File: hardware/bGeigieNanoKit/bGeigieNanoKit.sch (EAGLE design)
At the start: 34 parts, among them T1 2SC1815

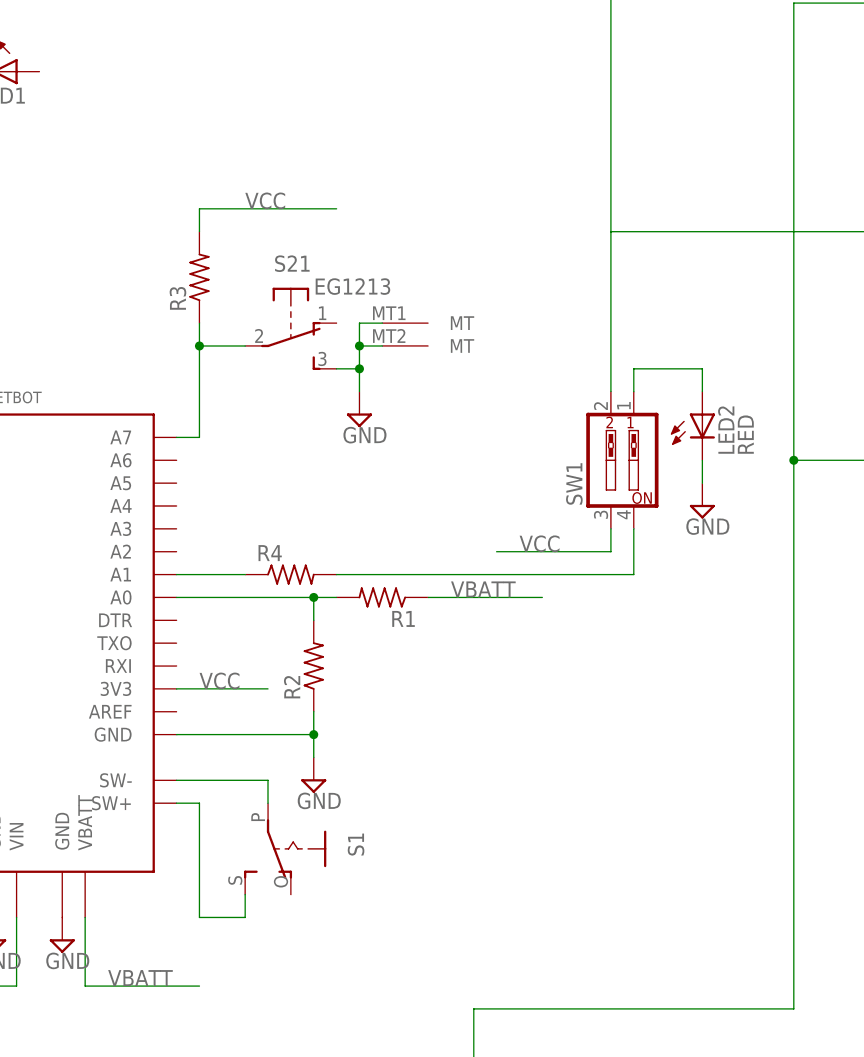
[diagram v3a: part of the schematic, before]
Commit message: resize board to be better fit in case. did inital pass at routing.
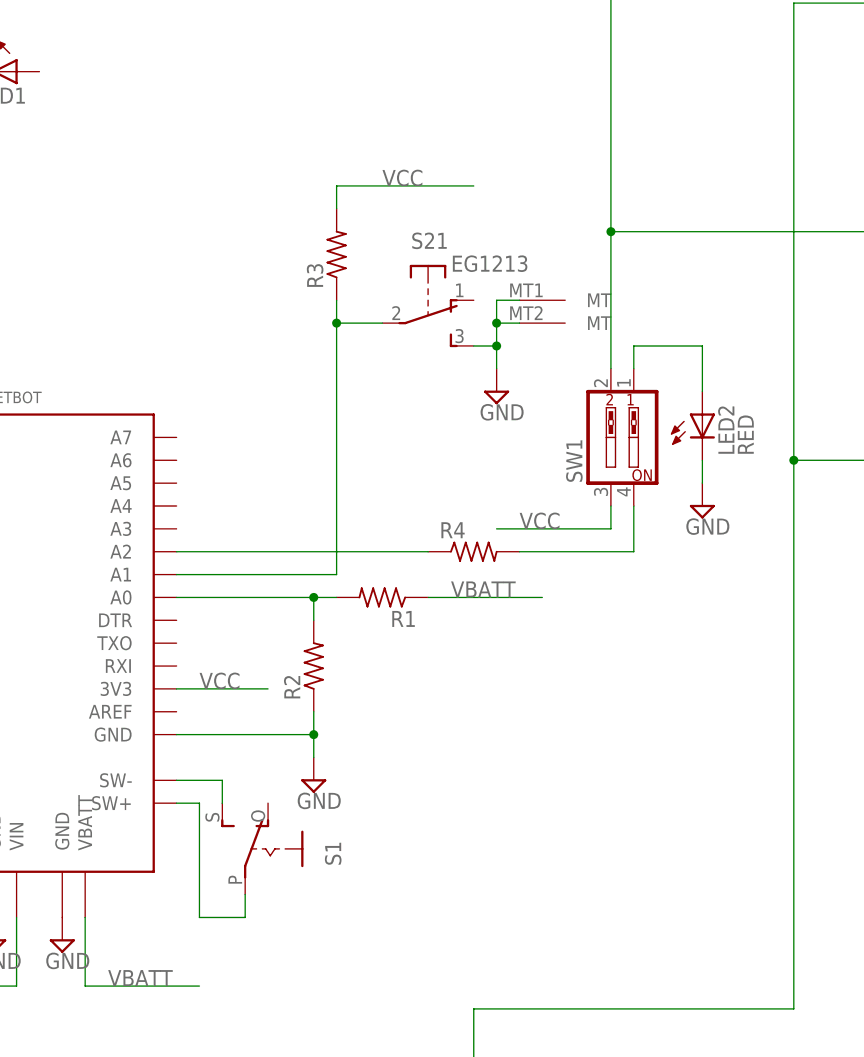
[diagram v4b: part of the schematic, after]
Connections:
- net N$12: now also S1.P; no longer S1.S
- net N$13: now also S1.S; no longer S1.P
- net N$14: now also U$2.A1; no longer U$2.A7
- net N$15: now also U$2.A2; no longer U$2.A1
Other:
- moved on the sheet: R3, R4, S1, S21, SW1
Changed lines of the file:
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@@
 </variantdefs>
 <classes>
-<class number="0" name="default" width="0" drill="0">
+<class number="0" name="default" width="0.3048" drill="0.254">
+<clearance class="0" value="0.3048"/>
 </class>
-<class number="1" name="PWP" width="0.254" drill="0.2032">
-<clearance class="1" value="0.254"/>
+<class number="1" name="PWP" width="0.4064" drill="0.254">
+<clearance class="1" value="0.3048"/>
+</class>
+<class number="2" name="HIGH_PWR" width="0.8128" drill="0.508">
+<clearance class="2" value="0.4064"/>
 </class>
 </classes>
@@
 <instance part="JP1" gate="A" x="30.48" y="40.64" rot="R180"/>
 <instance part="JP2" gate="A" x="256.54" y="106.68"/>
-<instance part="SW1" gate="G$1" x="175.26" y="109.22" rot="R90"/>
+<instance part="SW1" gate="G$1" x="175.26" y="111.76" rot="R90"/>
 <instance part="S5" gate="G$1" x="86.36" y="86.36" rot="MR0"/>
-<instance part="S1" gate="1" x="139.7" y="66.04" rot="R180"/>
+<instance part="S1" gate="1" x="137.16" y="66.04" rot="MR0"/>
 <instance part="SG1" gate="G$1" x="220.98" y="134.62" rot="R270"/>
 <instance part="U$5" gate="G$1" x="48.26" y="170.18" rot="MR0"/>
@@
 <instance part="SUPPLY8" gate="GND" x="114.3" y="55.88"/>
 <instance part="SUPPLY9" gate="GND" x="185.42" y="104.14"/>
-<instance part="SUPPLY10" gate="GND" x="147.32" y="114.3"/>
+<instance part="SUPPLY10" gate="GND" x="162.56" y="116.84"/>
 <instance part="R1" gate="G$1" x="149.86" y="93.98" rot="R180"/>
 <instance part="R2" gate="G$1" x="142.24" y="86.36" rot="R90"/>
-<instance part="R3" gate="G$1" x="129.54" y="129.54" rot="R90"/>
-<instance part="R4" gate="G$1" x="139.7" y="96.52"/>
+<instance part="R3" gate="G$1" x="144.78" y="132.08" rot="R90"/>
+<instance part="R4" gate="G$1" x="160.02" y="99.06"/>
 <instance part="R5" gate="G$1" x="213.36" y="160.02"/>
 <instance part="R6" gate="G$1" x="236.22" y="160.02"/>
@@
 <instance part="SUPPLY13" gate="GND" x="228.6" y="147.32"/>
 <instance part="SUPPLY14" gate="GND" x="248.92" y="152.4"/>
-<instance part="S2" gate="1" x="139.7" y="121.92" rot="R270"/>
-<instance part="S2" gate="G$1" x="149.86" y="124.46"/>
-<instance part="S2" gate="G$2" x="149.86" y="121.92"/>
+<instance part="S2" gate="1" x="154.94" y="124.46" rot="R270"/>
+<instance part="S2" gate="G$1" x="165.1" y="127"/>
+<instance part="S2" gate="G$2" x="165.1" y="124.46"/>
 <instance part="SUPPLY15" gate="GND" x="73.66" y="81.28"/>
 <instance part="H1" gate="G$1" x="198.12" y="27.94"/>
@@
 <segment>
 <pinref part="SUPPLY10" gate="GND" pin="GND"/>
-<wire x1="147.32" y1="116.84" x2="147.32" y2="119.38" width="0.1524" layer="91"/>
-<wire x1="147.32" y1="119.38" x2="144.78" y2="119.38" width="0.1524" layer="91"/>
+<wire x1="162.56" y1="119.38" x2="162.56" y2="121.92" width="0.1524" layer="91"/>
+<wire x1="162.56" y1="121.92" x2="160.02" y2="121.92" width="0.1524" layer="91"/>
 <pinref part="S2" gate="1" pin="S"/>
 <pinref part="S2" gate="G$1" pin="MT"/>
-<wire x1="149.86" y1="124.46" x2="147.32" y2="124.46" width="0.1524" layer="91"/>
-<wire x1="147.32" y1="124.46" x2="147.32" y2="121.92" width="0.1524" layer="91"/>
+<wire x1="165.1" y1="127" x2="162.56" y2="127" width="0.1524" layer="91"/>
+<wire x1="162.56" y1="127" x2="162.56" y2="124.46" width="0.1524" layer="91"/>
 <pinref part="S2" gate="G$2" pin="MT"/>
-<wire x1="147.32" y1="121.92" x2="147.32" y2="119.38" width="0.1524" layer="91"/>
-<wire x1="149.86" y1="121.92" x2="147.32" y2="121.92" width="0.1524" layer="91"/>
-<junction x="147.32" y="121.92"/>
-<junction x="147.32" y="119.38"/>
+<wire x1="162.56" y1="124.46" x2="162.56" y2="121.92" width="0.1524" layer="91"/>
+<wire x1="165.1" y1="124.46" x2="162.56" y2="124.46" width="0.1524" layer="91"/>
+<junction x="162.56" y="124.46"/>
+<junction x="162.56" y="121.92"/>
 </segment>
 <segment>
@@
 </segment>
 </net>
-<net name="VCC" class="0">
+<net name="VCC" class="1">
 <segment>
 <wire x1="127" y1="83.82" x2="137.16" y2="83.82" width="0.1524" layer="91"/>
@@
 <segment>
 <pinref part="R3" gate="G$1" pin="2"/>
-<wire x1="129.54" y1="134.62" x2="129.54" y2="137.16" width="0.1524" layer="91"/>
-<wire x1="129.54" y1="137.16" x2="144.78" y2="137.16" width="0.1524" layer="91"/>
-<label x="134.62" y="137.16" size="1.778" layer="95"/>
+<wire x1="144.78" y1="137.16" x2="144.78" y2="139.7" width="0.1524" layer="91"/>
+<wire x1="144.78" y1="139.7" x2="160.02" y2="139.7" width="0.1524" layer="91"/>
+<label x="149.86" y="139.7" size="1.778" layer="95"/>
 </segment>
 <segment>
@@
 <segment>
 <pinref part="SW1" gate="G$1" pin="3"/>
-<wire x1="175.26" y1="101.6" x2="175.26" y2="99.06" width="0.1524" layer="91"/>
-<wire x1="175.26" y1="99.06" x2="162.56" y2="99.06" width="0.1524" layer="91"/>
-<label x="165.1" y="99.06" size="1.778" layer="95"/>
+<wire x1="175.26" y1="104.14" x2="175.26" y2="101.6" width="0.1524" layer="91"/>
+<wire x1="175.26" y1="101.6" x2="162.56" y2="101.6" width="0.1524" layer="91"/>
+<label x="165.1" y="101.6" size="1.778" layer="95"/>
 </segment>
 </net>
@@
 </segment>
 </net>
-<net name="N$12" class="0">
+<net name="N$12" class="2">
 <segment>
 <pinref part="U$2" gate="G$1" pin="SW+"/>
@@
 <wire x1="129.54" y1="71.12" x2="129.54" y2="58.42" width="0.1524" layer="91"/>
 <wire x1="129.54" y1="58.42" x2="134.62" y2="58.42" width="0.1524" layer="91"/>
-<pinref part="S1" gate="1" pin="S"/>
+<pinref part="S1" gate="1" pin="P"/>
 <wire x1="134.62" y1="58.42" x2="134.62" y2="60.96" width="0.1524" layer="91"/>
 </segment>
@@
 </segment>
 </net>
-<net name="N$13" class="0">
+<net name="N$13" class="2">
 <segment>
 <pinref part="U$2" gate="G$1" pin="SW-"/>
-<wire x1="127" y1="73.66" x2="137.16" y2="73.66" width="0.1524" layer="91"/>
-<pinref part="S1" gate="1" pin="P"/>
-<wire x1="137.16" y1="71.12" x2="137.16" y2="73.66" width="0.1524" layer="91"/>
+<wire x1="127" y1="73.66" x2="132.08" y2="73.66" width="0.1524" layer="91"/>
+<pinref part="S1" gate="1" pin="S"/>
+<wire x1="132.08" y1="73.66" x2="132.08" y2="71.12" width="0.1524" layer="91"/>
 </segment>
 </net>
@@
 <net name="N$14" class="0">
 <segment>
-<wire x1="134.62" y1="121.92" x2="129.54" y2="121.92" width="0.1524" layer="91"/>
-<wire x1="129.54" y1="121.92" x2="129.54" y2="111.76" width="0.1524" layer="91"/>
-<pinref part="U$2" gate="G$1" pin="A7"/>
-<wire x1="129.54" y1="111.76" x2="127" y2="111.76" width="0.1524" layer="91"/>
+<wire x1="149.86" y1="124.46" x2="144.78" y2="124.46" width="0.1524" layer="91"/>
 <pinref part="R3" gate="G$1" pin="1"/>
-<wire x1="129.54" y1="124.46" x2="129.54" y2="121.92" width="0.1524" layer="91"/>
-<junction x="129.54" y="121.92"/>
+<wire x1="144.78" y1="127" x2="144.78" y2="124.46" width="0.1524" layer="91"/>
+<junction x="144.78" y="124.46"/>
 <pinref part="S2" gate="1" pin="P"/>
-</segment>
-</net>
-<net name="N$15" class="0">
-<segment>
+<wire x1="144.78" y1="96.52" x2="144.78" y2="124.46" width="0.1524" layer="91"/>
 <pinref part="U$2" gate="G$1" pin="A1"/>
-<pinref part="R4" gate="G$1" pin="1"/>
-<wire x1="127" y1="96.52" x2="134.62" y2="96.52" width="0.1524" layer="91"/>
+<wire x1="144.78" y1="96.52" x2="127" y2="96.52" width="0.1524" layer="91"/>
 </segment>
 </net>
@@
 <segment>
 <pinref part="R4" gate="G$1" pin="2"/>
-<wire x1="144.78" y1="96.52" x2="177.8" y2="96.52" width="0.1524" layer="91"/>
+<wire x1="165.1" y1="99.06" x2="177.8" y2="99.06" width="0.1524" layer="91"/>
 <pinref part="SW1" gate="G$1" pin="4"/>
-<wire x1="177.8" y1="96.52" x2="177.8" y2="101.6" width="0.1524" layer="91"/>
+<wire x1="177.8" y1="99.06" x2="177.8" y2="104.14" width="0.1524" layer="91"/>
 </segment>
 </net>
@@
 <wire x1="218.44" y1="134.62" x2="175.26" y2="134.62" width="0.1524" layer="91"/>
 <pinref part="SW1" gate="G$1" pin="2"/>
-<wire x1="175.26" y1="134.62" x2="175.26" y2="116.84" width="0.1524" layer="91"/>
+<wire x1="175.26" y1="134.62" x2="175.26" y2="119.38" width="0.1524" layer="91"/>
+<junction x="175.26" y="134.62"/>
 </segment>
 </net>
@@
 <segment>
 <pinref part="SW1" gate="G$1" pin="1"/>
-<wire x1="177.8" y1="116.84" x2="177.8" y2="119.38" width="0.1524" layer="91"/>
-<wire x1="177.8" y1="119.38" x2="185.42" y2="119.38" width="0.1524" layer="91"/>
+<wire x1="177.8" y1="119.38" x2="177.8" y2="121.92" width="0.1524" layer="91"/>
+<wire x1="177.8" y1="121.92" x2="185.42" y2="121.92" width="0.1524" layer="91"/>
 <pinref part="LED2" gate="G$1" pin="A"/>
-<wire x1="185.42" y1="119.38" x2="185.42" y2="116.84" width="0.1524" layer="91"/>
+<wire x1="185.42" y1="121.92" x2="185.42" y2="116.84" width="0.1524" layer="91"/>
 </segment>
 </net>
@@
 </segment>
 </net>
+<net name="N$15" class="0">
+<segment>
+<pinref part="R4" gate="G$1" pin="1"/>
+<pinref part="U$2" gate="G$1" pin="A2"/>
+<wire x1="154.94" y1="99.06" x2="127" y2="99.06" width="0.1524" layer="91"/>
+</segment>
+</net>

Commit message: fully routed board
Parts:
- removed H1, H2, H3, H4: MOUNT-HOLE3.0, holes:MOUNT-HOLE3.0
- removed LED3: (no value), adafruit:LED3MM
- removed S2: EG1213, adafruit:EG1213
- added S3: (no value), adafruit:EG1218S
- added U$6, U$7, U$8, U$9: MOUNTINGHOLE3.0THIN, microbuilder:MOUNTINGHOLE3.0THIN
- SW1: device SparkFun:SW_DIP-2 -> special:SW_DIP-2
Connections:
- net GND: now also S3.S; no longer S21.S, S2G$1.MT, S2G$2.MT
- net N$14: now also S3.P, U$2.A7; no longer S21.P, U$2.A1
- net N$19: now also LED1.A, R7.2; no longer LED3.A, R7.1
- net N$21: now also R7.1; no longer R7.2
- net N$22: now also LED1.C; no longer LED3.C
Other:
- moved on the sheet: C1, C2, C3, D1, JP1, JP2, LED1, LED2, R1, R10, R2, R3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

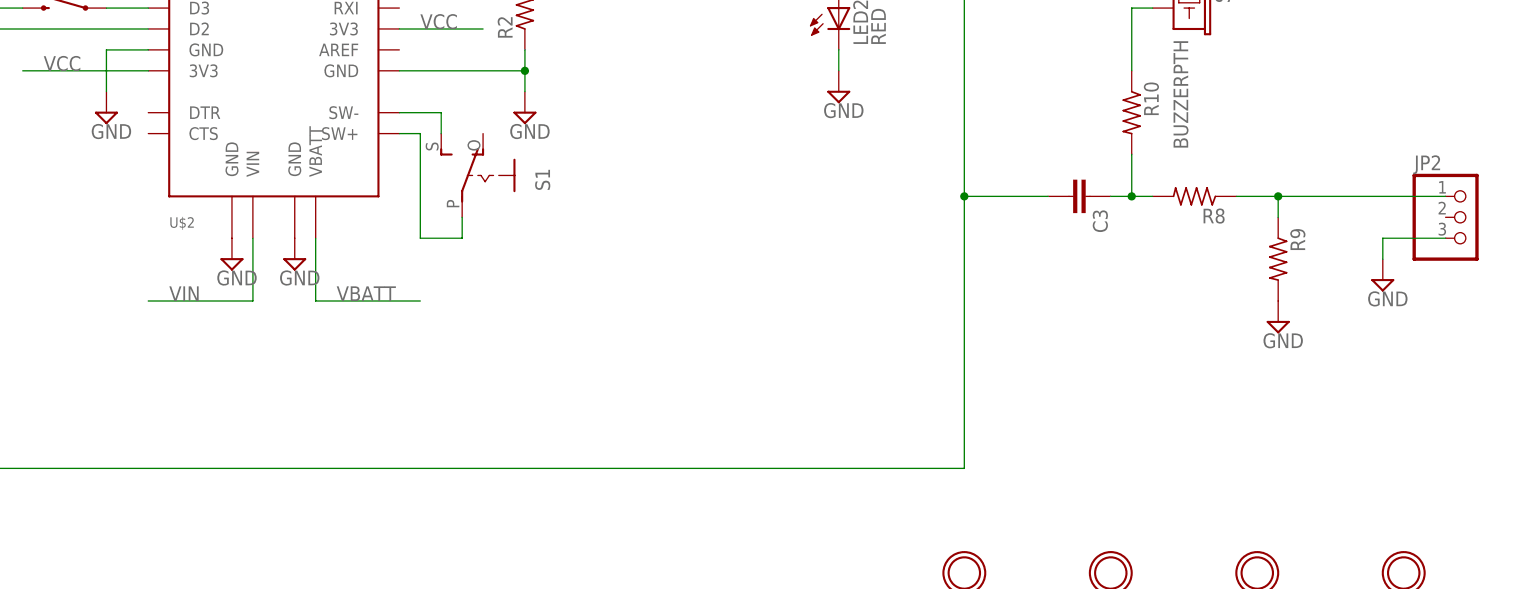
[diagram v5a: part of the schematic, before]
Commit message: cleaned up final routing
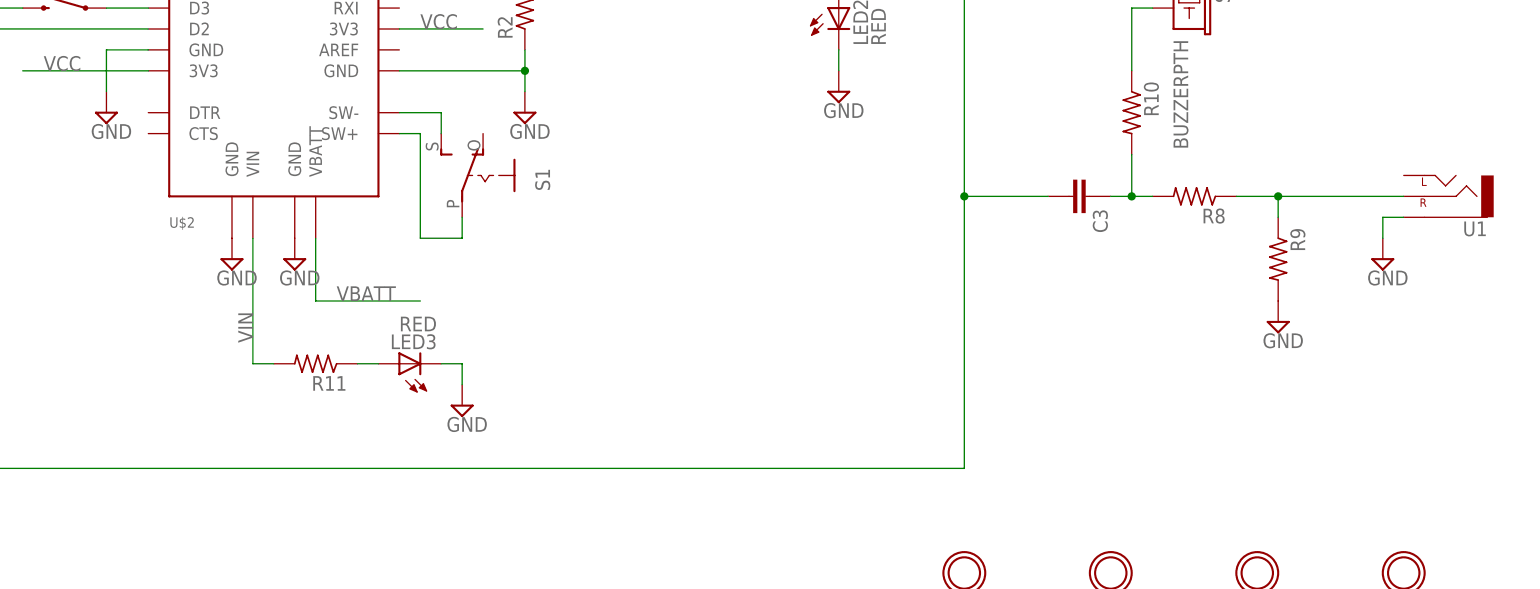
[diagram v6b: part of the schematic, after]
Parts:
- removed JP2: (no value), microbuilder:HEADER-1X376MIL
- added LED3: RED, adafruit:LED3MM
- added R11: (no value), rcl:R-US_0207/10
- added U1: (no value), SparkFun:AUDIO-JACK2.5MM
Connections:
- new net N$29: LED3.A, R11.1
- net GND: now also LED3.C, U1.SLEEVE; no longer JP2.3
- net N$25: now also U1.RIGHT; no longer JP2.1
- net VIN: now also R11.2
